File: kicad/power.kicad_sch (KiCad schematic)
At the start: 0 parts

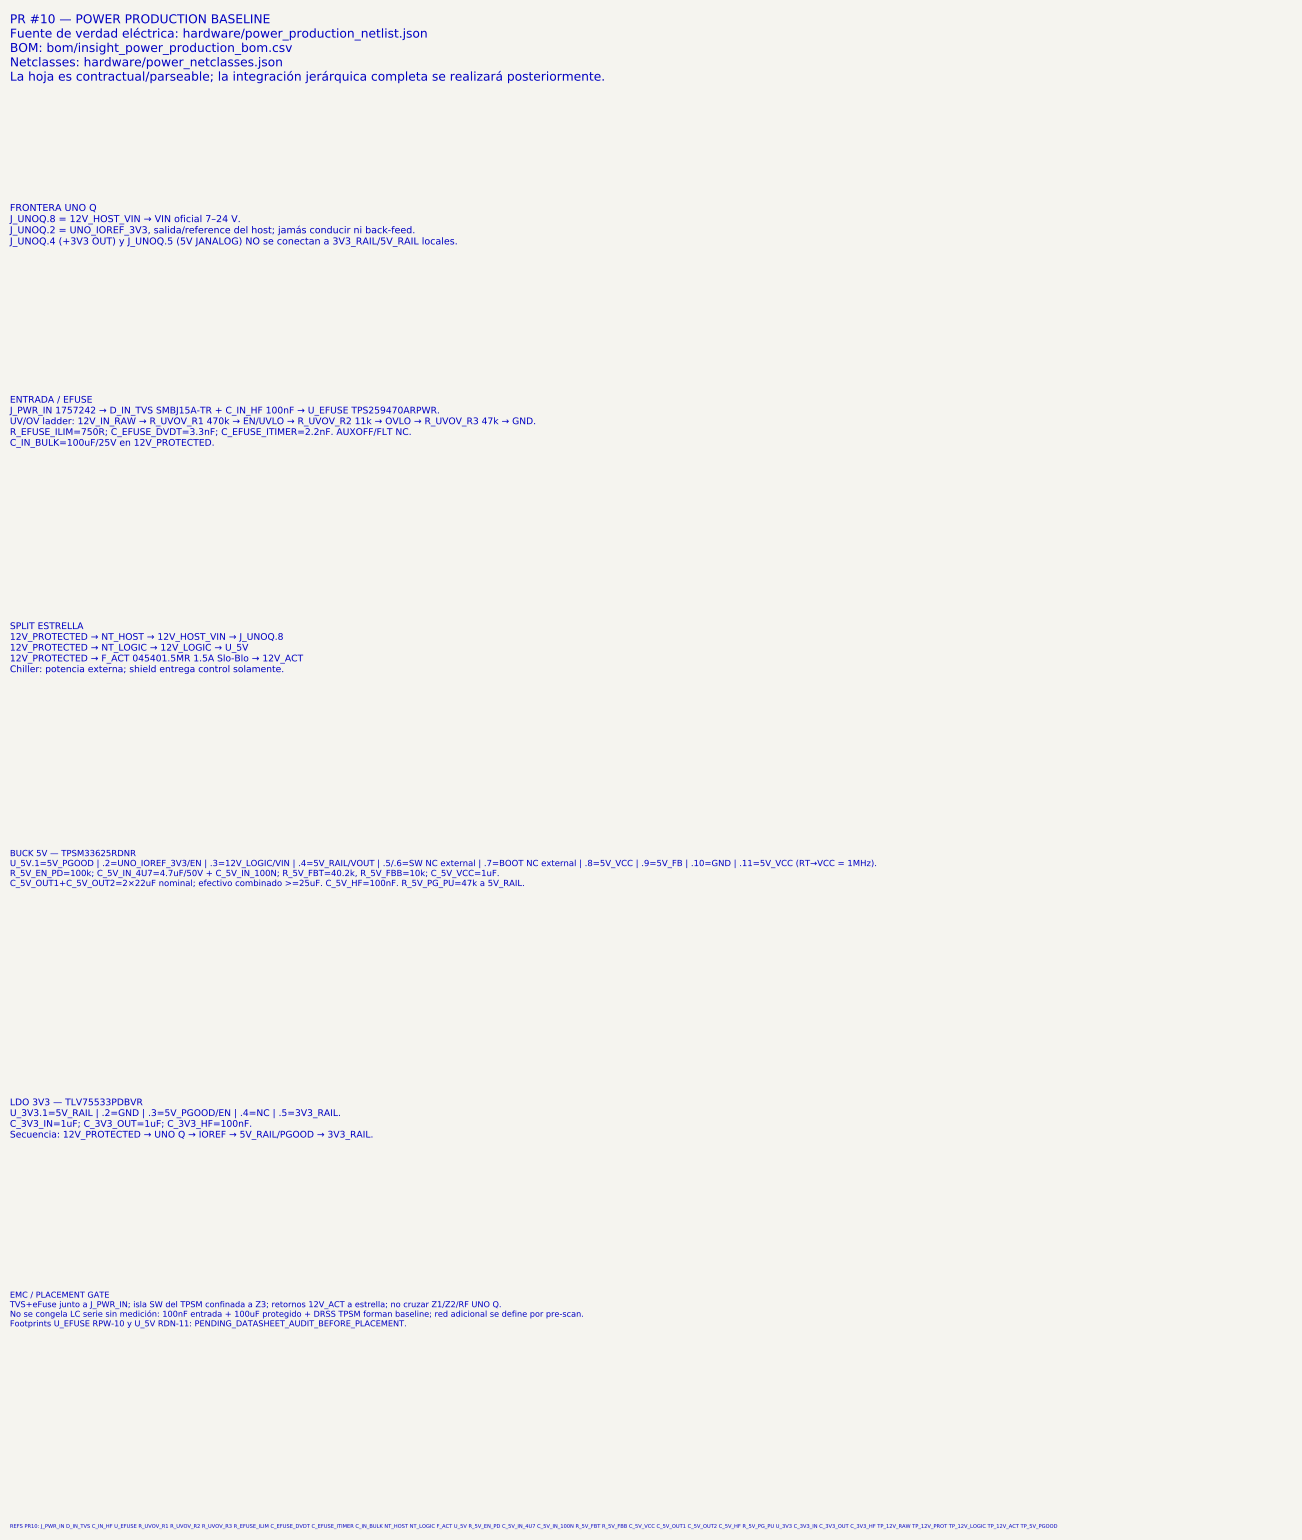
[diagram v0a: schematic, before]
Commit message: eda: actualizar hoja de potencia con footprints cerrados PR13
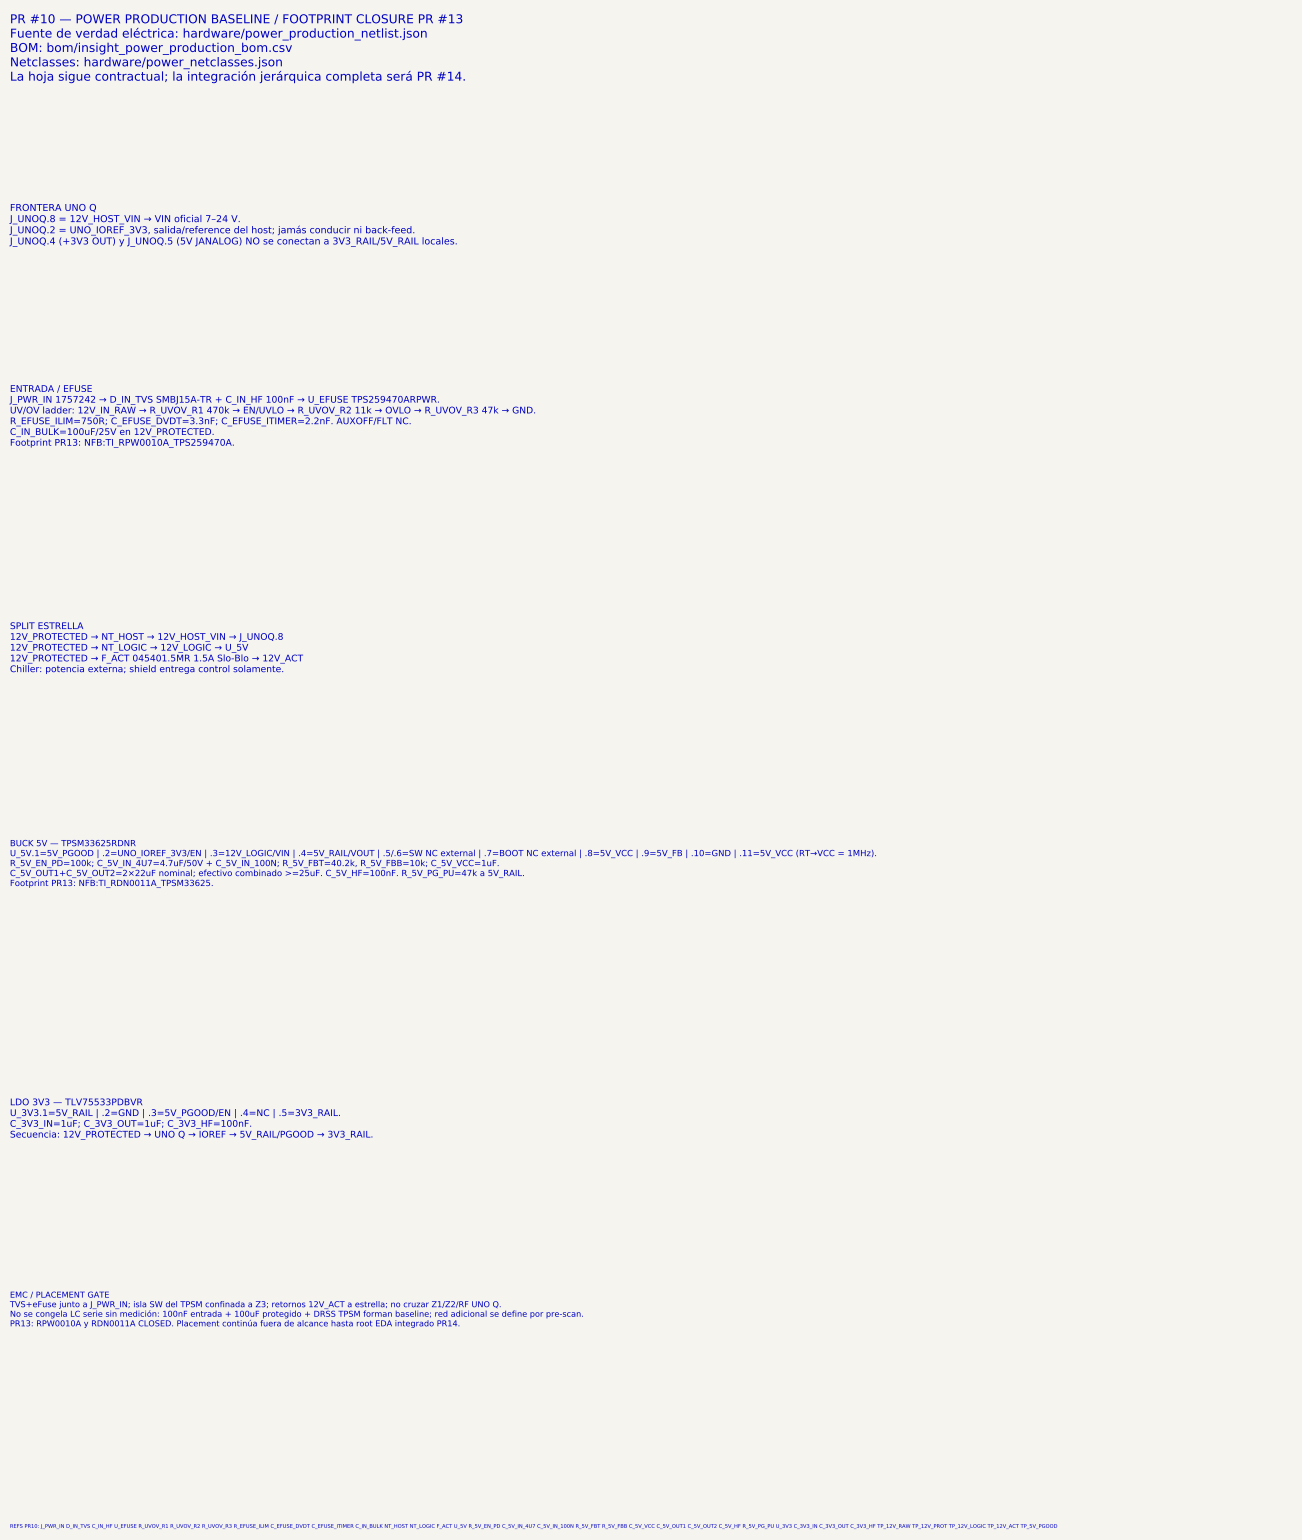
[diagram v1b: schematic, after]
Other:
- note added: "EMC / PLACEMENT GATE TVS+eFuse junto a J_PWR_IN; isla SW del TPSM confinada a Z3; retornos 12V_ACT a estrella; no cruzar Z1/Z2/RF UNO Q. No se congela LC serie sin medición: 100nF entrada + 100uF protegido + DRSS TPSM forman baseline; red adicional se define por pre-scan. PR13: RPW0010A y RDN0011A CLOSED. Placement continúa fuera de alcance hasta root EDA integrado PR14."
- note added: "ENTRADA / EFUSE J_PWR_IN 1757242 → D_IN_TVS SMBJ15A-TR + C_IN_HF 100nF → U_EFUSE TPS259470ARPWR. UV/OV ladder: 12V_IN_RAW → R_UVOV_R1 470k → EN/UVLO → R_UVOV_R2 11k → OVLO → R_UVOV_R3 47k → GND. R_EFUSE_ILIM=750R; C_EFUSE_DVDT=3.3nF; C_EFUSE_ITIMER=2.2nF. AUXOFF/FLT NC. C_IN_BULK=100uF/25V en 12V_PROTECTED. Footprint PR13: NFB:TI_RPW0010A_TPS259470A."
- note added: "PR #10 — POWER PRODUCTION BASELINE / FOOTPRINT CLOSURE PR #13 Fuente de verdad eléctrica: hardware/power_production_netlist.json BOM: bom/insight_power_production_bom.csv Netclasses: hardware/power_netclasses.json La hoja sigue contractual; la integración jerárquica completa será PR #14."
- note removed: "EMC / PLACEMENT GATE TVS+eFuse junto a J_PWR_IN; isla SW del TPSM confinada a Z3; retornos 12V_ACT a estrella; no cruzar Z1/Z2/RF UNO Q. No se congela LC serie sin medición: 100nF entrada + 100uF protegido + DRSS TPSM forman baseline; red adicional se define por pre-scan. Footprints U_EFUSE RPW-10 y U_5V RDN-11: PENDING_DATASHEET_AUDIT_BEFORE_PLACEMENT."
- note removed: "ENTRADA / EFUSE J_PWR_IN 1757242 → D_IN_TVS SMBJ15A-TR + C_IN_HF 100nF → U_EFUSE TPS259470ARPWR. UV/OV ladder: 12V_IN_RAW → R_UVOV_R1 470k → EN/UVLO → R_UVOV_R2 11k → OVLO → R_UVOV_R3 47k → GND. R_EFUSE_ILIM=750R; C_EFUSE_DVDT=3.3nF; C_EFUSE_ITIMER=2.2nF. AUXOFF/FLT NC. C_IN_BULK=100uF/25V en 12V_PROTECTED."
- note removed: "PR #10 — POWER PRODUCTION BASELINE Fuente de verdad eléctrica: hardware/power_production_netlist.json BOM: bom/insight_power_production_bom.csv Netclasses: hardware/power_netclasses.json La hoja es contractual/parseable; la integración jerárquica completa se realizará posteriormente."
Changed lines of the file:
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@@
   (version 20250114)
   (generator "nfb_pr10_power_contract")
-  (generator_version "1.0")
+  (generator_version "1.1")
   (paper "A3")
   (title_block
     (title "NFB Insight PCBA v2 — Power Production Contract")
-    (date "2026-08-11")
-    (rev "0.10.0")
+    (date "2026-08-12")
+    (rev "0.13.0")
     (company "Cafelium SRL / Nebula Ecosystem")
-    (comment 1 "PR #10 — fuente eléctrica: hardware/power_production_netlist.json")
+    (comment 1 "PR #10 electrical baseline; footprints físicos cerrados por PR #13")
     (comment 2 "Arquitectura: hardware/power_architecture_contract.json")
-    (comment 3 "Sin placement ni routing; footprints RPW/RDN requieren auditoría")
+    (comment 3 "Sin placement ni routing; U_EFUSE/U_5V usan footprints NFB auditados")
     (comment 4 "UNO Q: fuentes primarias oficiales arduino/* según docs/SOURCE_OF_TRUTH.md")
   )
-  (text "PR #10 — POWER PRODUCTION BASELINE\nFuente de verdad eléctrica: hardware/power_production_netlist.json\nBOM: bom/insight_power_production_bom.csv\nNetclasses: hardware/power_netclasses.json\nLa hoja es contractual/parseable; la integración jerárquica completa se realizará posteriormente."
+  (text "PR #10 — POWER PRODUCTION BASELINE / FOOTPRINT CLOSURE PR #13\nFuente de verdad eléctrica: hardware/power_production_netlist.json\nBOM: bom/insight_power_production_bom.csv\nNetclasses: hardware/power_netclasses.json\nLa hoja sigue contractual; la integración jerárquica completa será PR #14."
     (exclude_from_sim no)
     (at 30.48 30.48 0)
@@
     (effects (font (size 1.4 1.4)) (justify left bottom))
   )
-  (text "ENTRADA / EFUSE\nJ_PWR_IN 1757242 → D_IN_TVS SMBJ15A-TR + C_IN_HF 100nF → U_EFUSE TPS259470ARPWR.\nUV/OV ladder: 12V_IN_RAW → R_UVOV_R1 470k → EN/UVLO → R_UVOV_R2 11k → OVLO → R_UVOV_R3 47k → GND.\nR_EFUSE_ILIM=750R; C_EFUSE_DVDT=3.3nF; C_EFUSE_ITIMER=2.2nF. AUXOFF/FLT NC.\nC_IN_BULK=100uF/25V en 12V_PROTECTED."
+  (text "ENTRADA / EFUSE\nJ_PWR_IN 1757242 → D_IN_TVS SMBJ15A-TR + C_IN_HF 100nF → U_EFUSE TPS259470ARPWR.\nUV/OV ladder: 12V_IN_RAW → R_UVOV_R1 470k → EN/UVLO → R_UVOV_R2 11k → OVLO → R_UVOV_R3 47k → GND.\nR_EFUSE_ILIM=750R; C_EFUSE_DVDT=3.3nF; C_EFUSE_ITIMER=2.2nF. AUXOFF/FLT NC.\nC_IN_BULK=100uF/25V en 12V_PROTECTED.\nFootprint PR13: NFB:TI_RPW0010A_TPS259470A."
     (exclude_from_sim no)
     (at 30.48 104.14 0)
@@
     (effects (font (size 1.35 1.35)) (justify left bottom))
   )
-  (text "BUCK 5V — TPSM33625RDNR\nU_5V.1=5V_PGOOD | .2=UNO_IOREF_3V3/EN | .3=12V_LOGIC/VIN | .4=5V_RAIL/VOUT | .5/.6=SW NC external | .7=BOOT NC external | .8=5V_VCC | .9=5V_FB | .10=GND | .11=5V_VCC (RT→VCC = 1MHz).\nR_5V_EN_PD=100k; C_5V_IN_4U7=4.7uF/50V + C_5V_IN_100N; R_5V_FBT=40.2k, R_5V_FBB=10k; C_5V_VCC=1uF.\nC_5V_OUT1+C_5V_OUT2=2×22uF nominal; efectivo combinado >=25uF. C_5V_HF=100nF. R_5V_PG_PU=47k a 5V_RAIL."
+  (text "BUCK 5V — TPSM33625RDNR\nU_5V.1=5V_PGOOD | .2=UNO_IOREF_3V3/EN | .3=12V_LOGIC/VIN | .4=5V_RAIL/VOUT | .5/.6=SW NC external | .7=BOOT NC external | .8=5V_VCC | .9=5V_FB | .10=GND | .11=5V_VCC (RT→VCC = 1MHz).\nR_5V_EN_PD=100k; C_5V_IN_4U7=4.7uF/50V + C_5V_IN_100N; R_5V_FBT=40.2k, R_5V_FBB=10k; C_5V_VCC=1uF.\nC_5V_OUT1+C_5V_OUT2=2×22uF nominal; efectivo combinado >=25uF. C_5V_HF=100nF. R_5V_PG_PU=47k a 5V_RAIL.\nFootprint PR13: NFB:TI_RDN0011A_TPSM33625."
     (exclude_from_sim no)
     (at 30.48 193.04 0)
@@
     (effects (font (size 1.35 1.35)) (justify left bottom))
   )
-  (text "EMC / PLACEMENT GATE\nTVS+eFuse junto a J_PWR_IN; isla SW del TPSM confinada a Z3; retornos 12V_ACT a estrella; no cruzar Z1/Z2/RF UNO Q.\nNo se congela LC serie sin medición: 100nF entrada + 100uF protegido + DRSS TPSM forman baseline; red adicional se define por pre-scan.\nFootprints U_EFUSE RPW-10 y U_5V RDN-11: PENDING_DATASHEET_AUDIT_BEFORE_PLACEMENT."
+  (text "EMC / PLACEMENT GATE\nTVS+eFuse junto a J_PWR_IN; isla SW del TPSM confinada a Z3; retornos 12V_ACT a estrella; no cruzar Z1/Z2/RF UNO Q.\nNo se congela LC serie sin medición: 100nF entrada + 100uF protegido + DRSS TPSM forman baseline; red adicional se define por pre-scan.\nPR13: RPW0010A y RDN0011A CLOSED. Placement continúa fuera de alcance hasta root EDA integrado PR14."
     (exclude_from_sim no)
     (at 30.48 281.94 0)
